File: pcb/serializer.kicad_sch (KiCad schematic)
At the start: 26 parts, among them U7 DS90UB953A-Q1

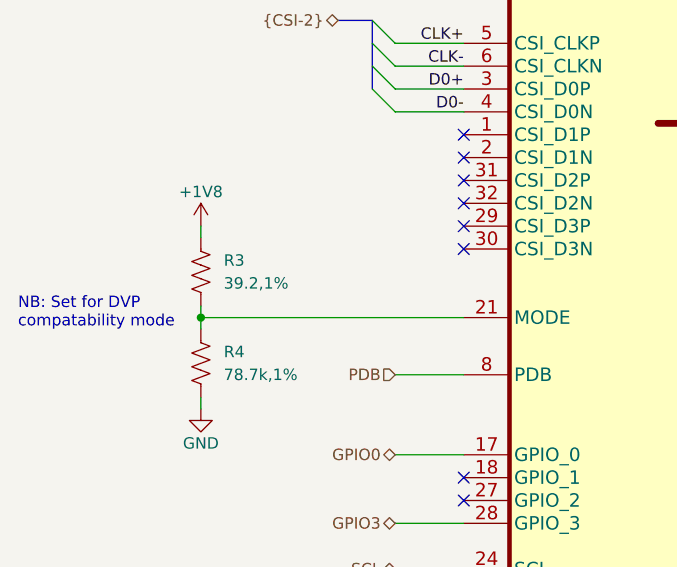
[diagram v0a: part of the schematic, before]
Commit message: PCB Revision A
- Added production files from Speedy
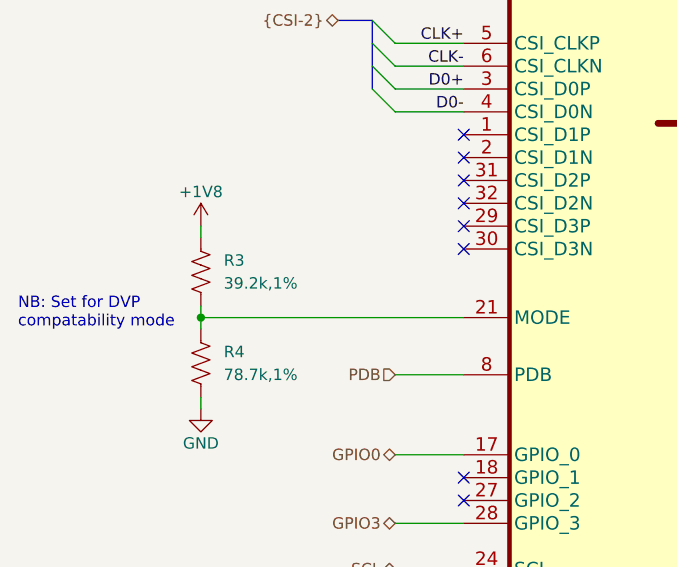
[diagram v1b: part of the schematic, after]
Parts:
- R3: value 39.2,1% -> 39.2k,1%
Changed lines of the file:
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@@
       (effects (font (size 1.27 1.27)) (justify left))
     )
-    (property "Value" "39.2,1%" (id 1) (at 81.28 125.73 0)
+    (property "Value" "39.2k,1%" (id 1) (at 81.28 125.73 0)
       (effects (font (size 1.27 1.27)) (justify left))
     )

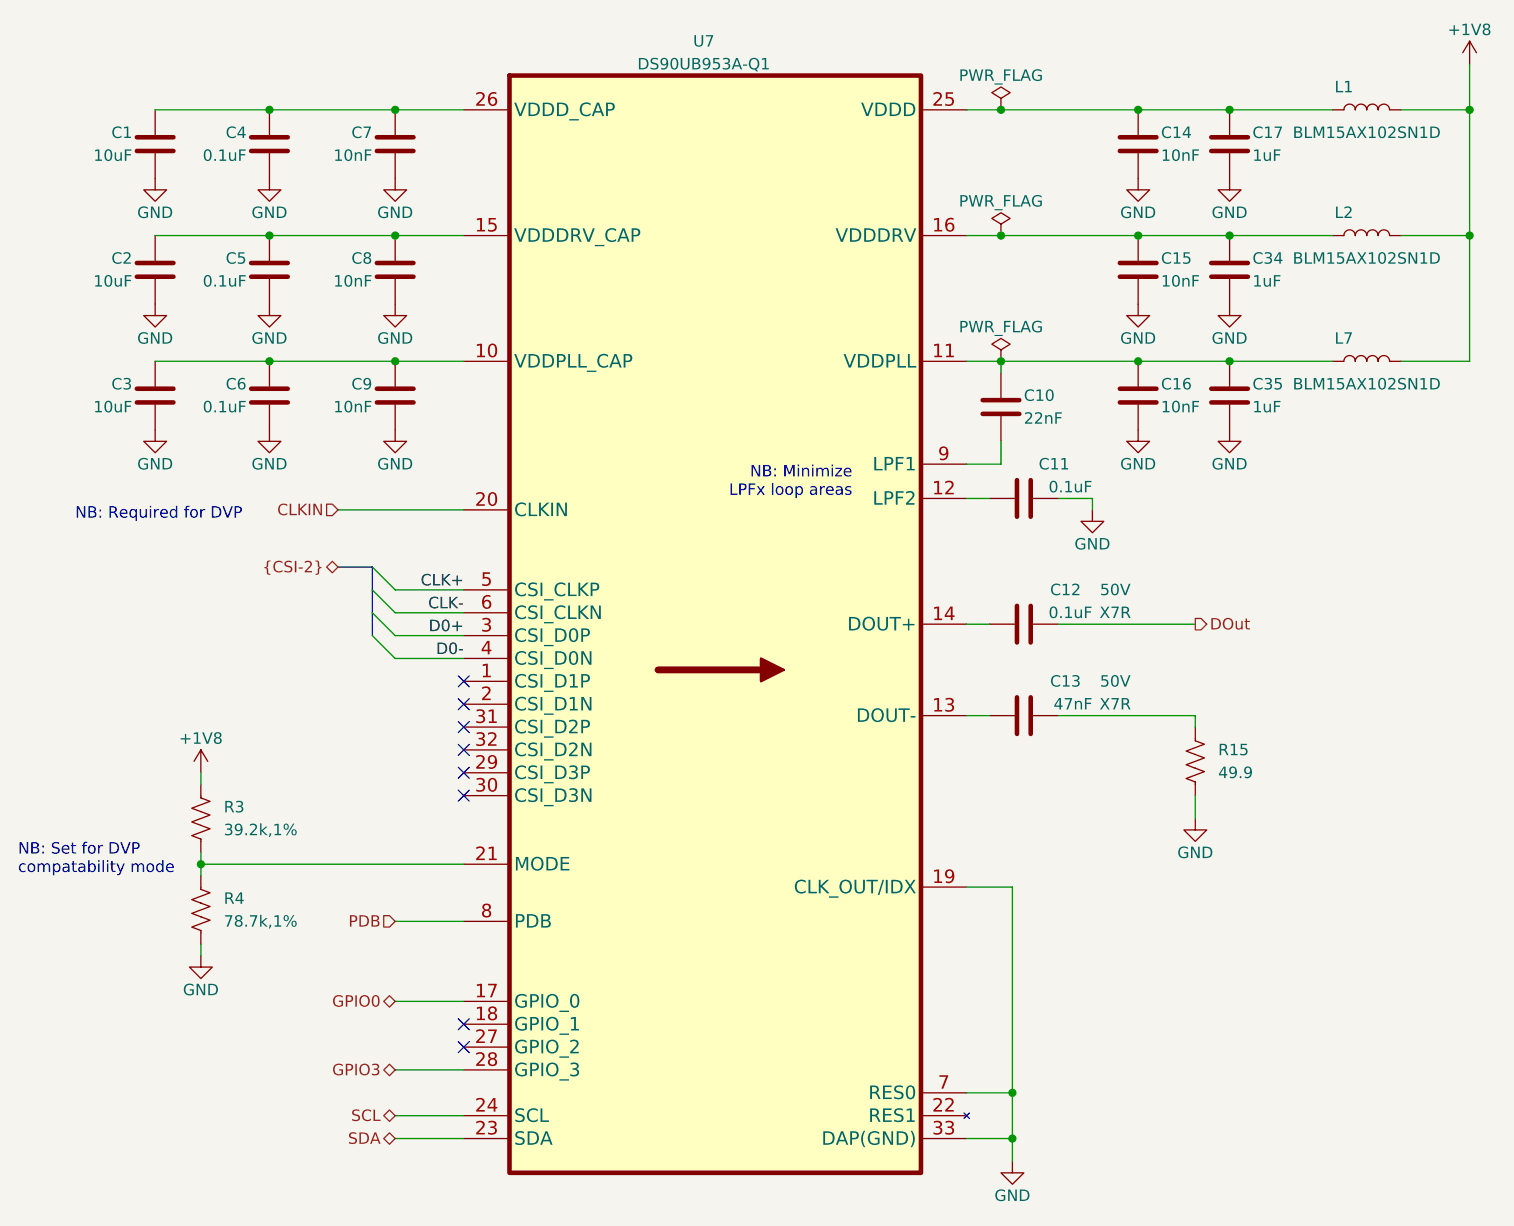
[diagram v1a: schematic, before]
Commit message: Revision B
- Bring in changes from headstage-rhs116 rev. C that should make this design
  fully functional
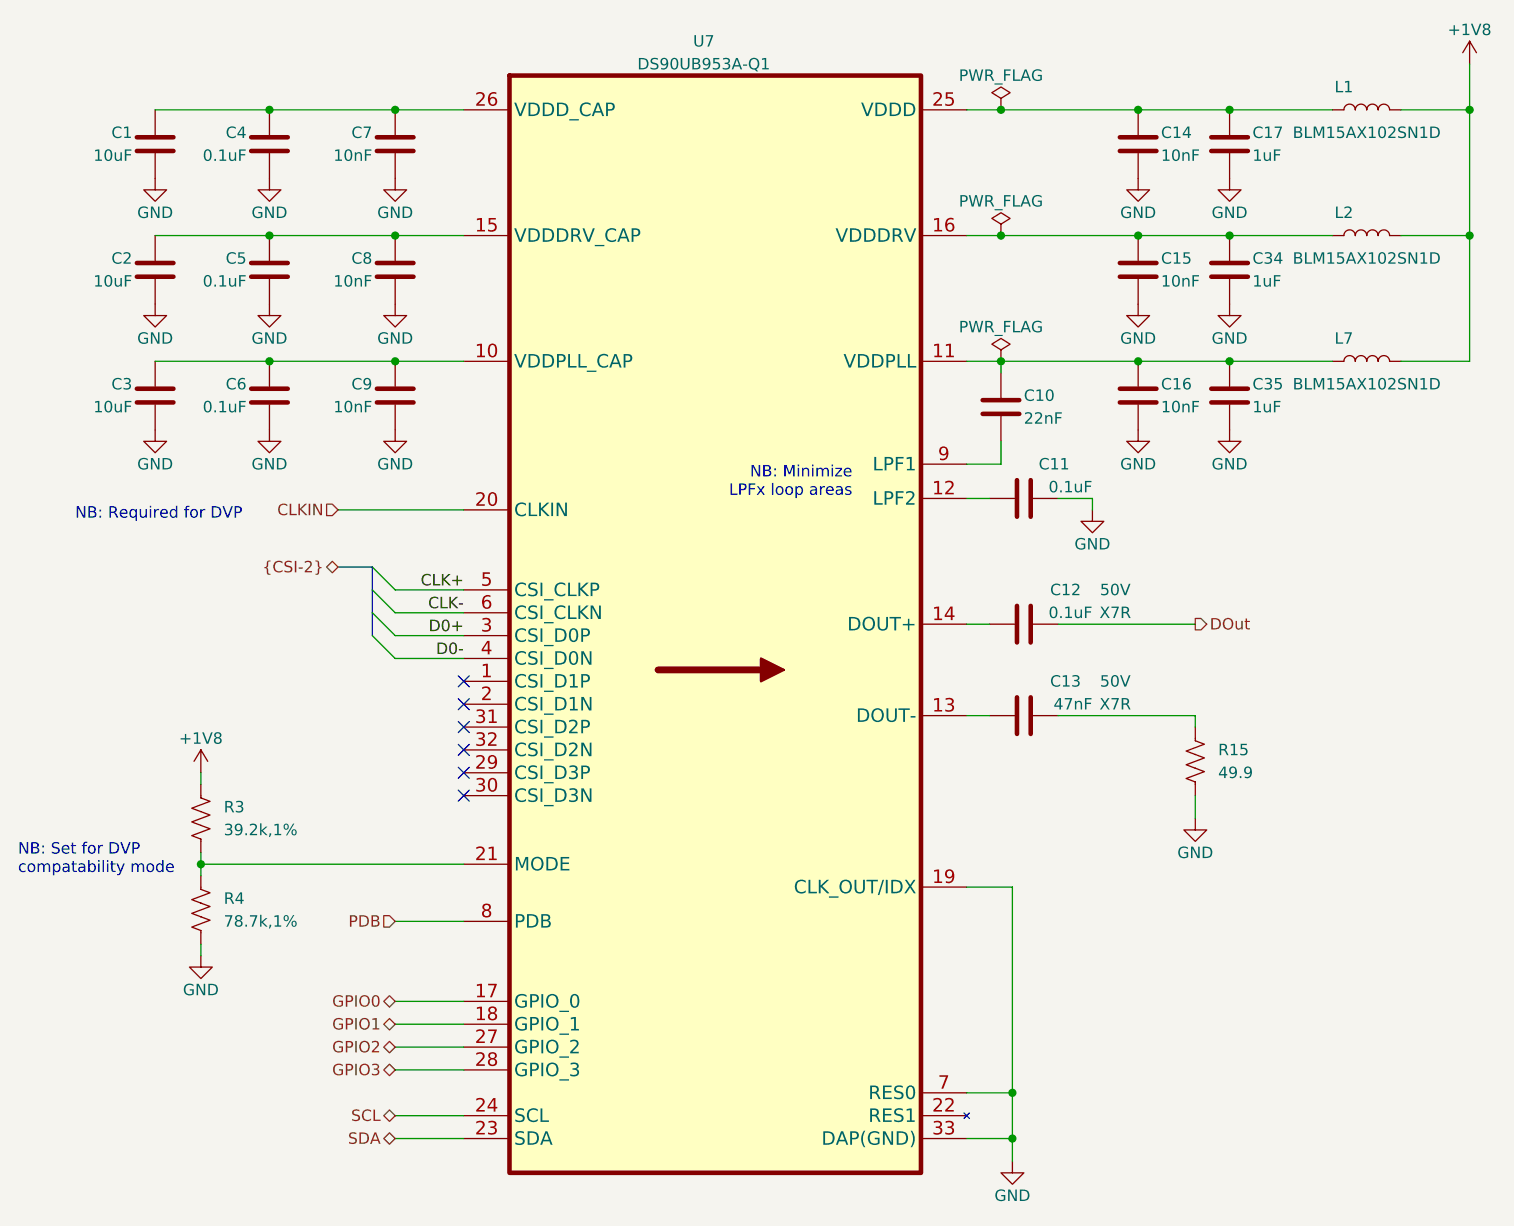
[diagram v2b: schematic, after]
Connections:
- net GPIO1: now reaches U7.18 (GPIO_1)
- net GPIO2: now reaches U7.27 (GPIO_2)
- no-connect marks 8 -> 6
